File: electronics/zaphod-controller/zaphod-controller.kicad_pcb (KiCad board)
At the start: 2 copper layers, 235 parts, among them P1 MOLEX_43160-0102, P10 CONN_01X01, P11 MOLEX_MINIFIT_JR_2x4_WAY, P12 MOLEX_MINIFIT_JR_2x4_WAY, P13 MOLEX_MINIFIT_JR_2x4_WAY, P14 MOLEX_MINIFIT_JR_2x4_WAY, P17 CONN_01X02, P18 CONN_01X02, P19 CONN_01X02, P2 MOLEX_MINIFIT_JR_2x2_WAY, P20 CONN_01X06, P21 CONN_01X02, P22 CONN_01X02, P23 MOLEX_KK2.54_1x4_WAY_FAN, P3 MOLEX_MINIFIT_JR_2x2_WAY, P4 MOLEX_MINIFIT_JR_2x2_WAY, P5 MOLEX_MINIFIT_JR_2x2_WAY, P6 CONN_01X04, P7 CONN_01X04, P8 CONN_01X04, P9 CONN_01X04, Q1 Si7852DP, Q2 Si7852DP, Q3 2N7002P, Q4 NTR1P02T1G, Q5 BC847B, Q6 2N7002P, SW1 B3U-1000P_SPST-NO_SMD, SW2 B3U-1000P_SPST-NO_SMD, SW3 B3U-1000P_SPST-NO_SMD, U1 ISL85410FRZ, U10 ULN2003A, U11 ULN2003A, U2 LM5116, U3 ISL85410FRZ, U4 STM32F429VET6, U5 USBLC6, U6 ACS711KEXLT_15AB, U7 ACS711KEXLT_15AB, U8 ACS711KEXLT_15AB, U9 ACS711KEXLT_15AB, X1 CSTCE8M00G55Z, X2 SWD_SMT_SOCKET, X3 ABS06-107-32.768KHZ

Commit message: PCB layout
Mostly grouping parts and testing layout concepts
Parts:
- moved P10 131.8 mm to (113.6, 68.0)
- moved C35 106.5 mm to (183.2, 86.6)
- moved C41 104.4 mm to (169.0, 89.2)
- moved FID1 100.0 mm to (227.7, 139.3)
- moved FID2 100.0 mm to (236.2, 137.6)
- moved FID3 100.0 mm to (229.4, 135.6)
- moved FID4 100.0 mm to (232.7, 136.3)
- moved R56 95.4 mm to (157.2, 115.0), turned to 180 degrees
- moved C48 92.7 mm to (181.6, 96.8)
- moved TEST8 90.2 mm to (165.2, 76.8)
- moved SW1 88.1 mm to (170.2, 105.6), turned to 180 degrees
- moved C45 86.4 mm to (179.8, 87.2), turned to 270 degrees
- moved D5 85.8 mm to (180.2, 118.6), turned to 90 degrees
- moved X1 85.7 mm to (178.2, 92.4), turned to 90 degrees
- moved C34 85.1 mm to (156.8, 80.0), turned to 180 degrees
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
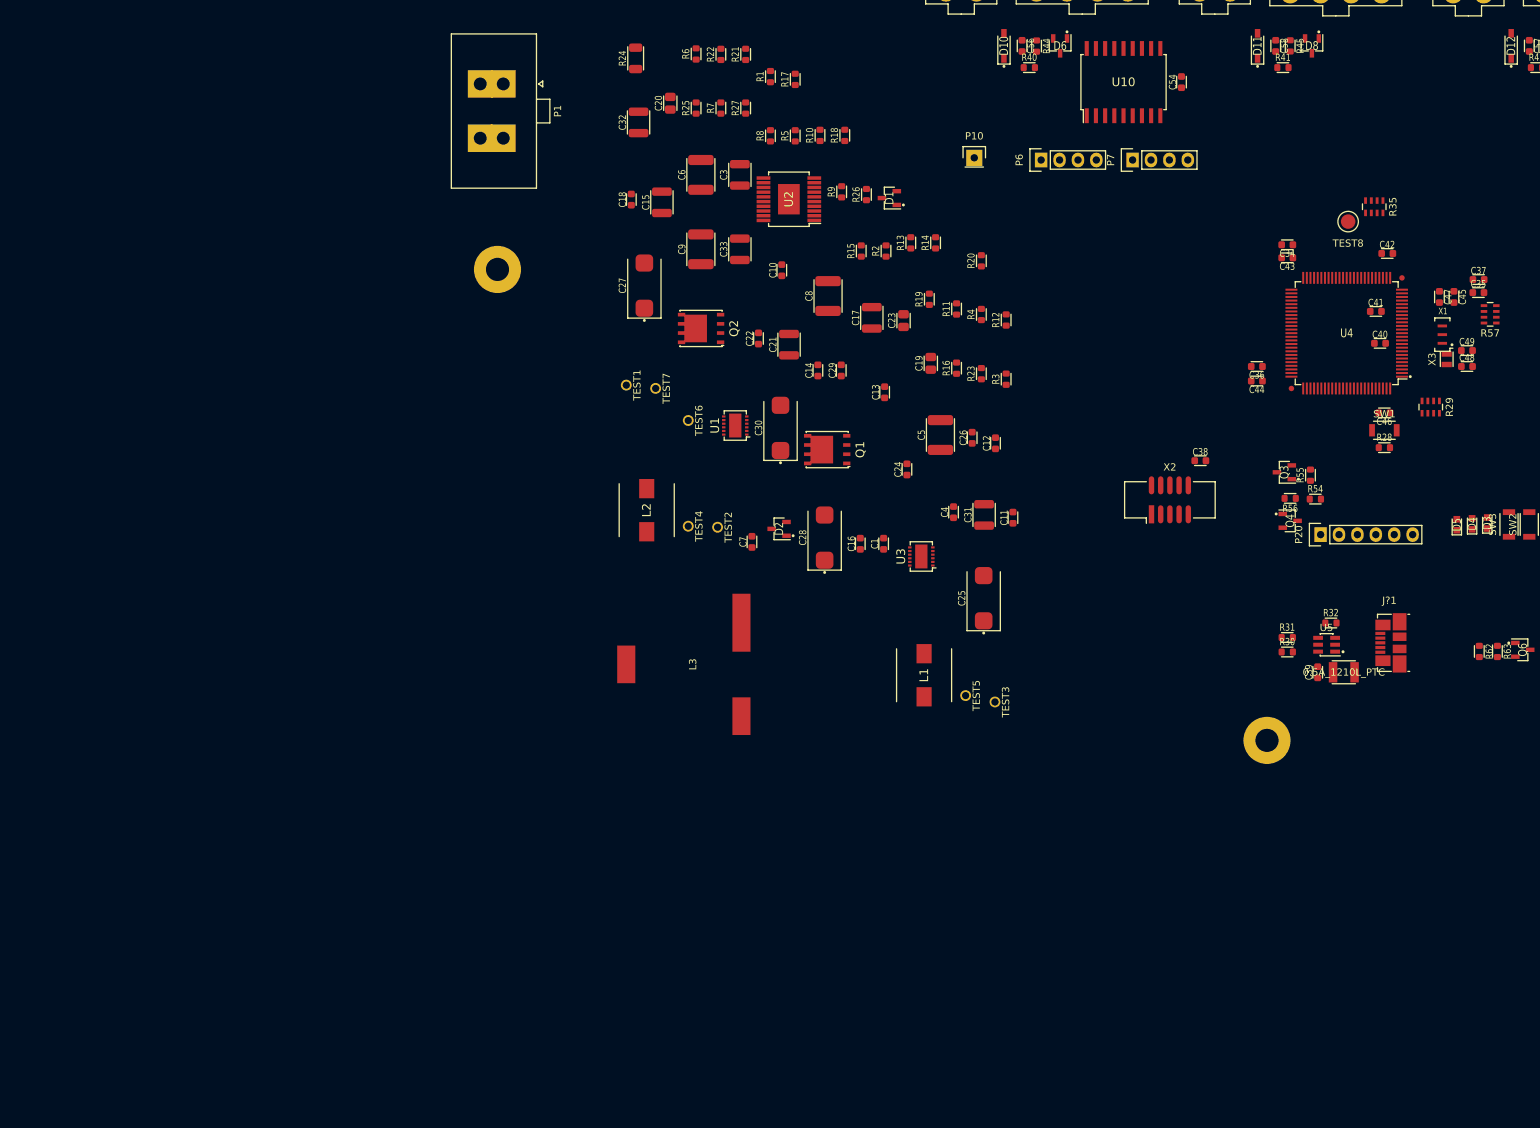
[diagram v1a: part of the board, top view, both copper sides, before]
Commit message: Placement refinement of 1A regulators
Removed some redundant parts, placed 3 and 5V regs.
Conjoined a few 1k resistors into quad arrays.
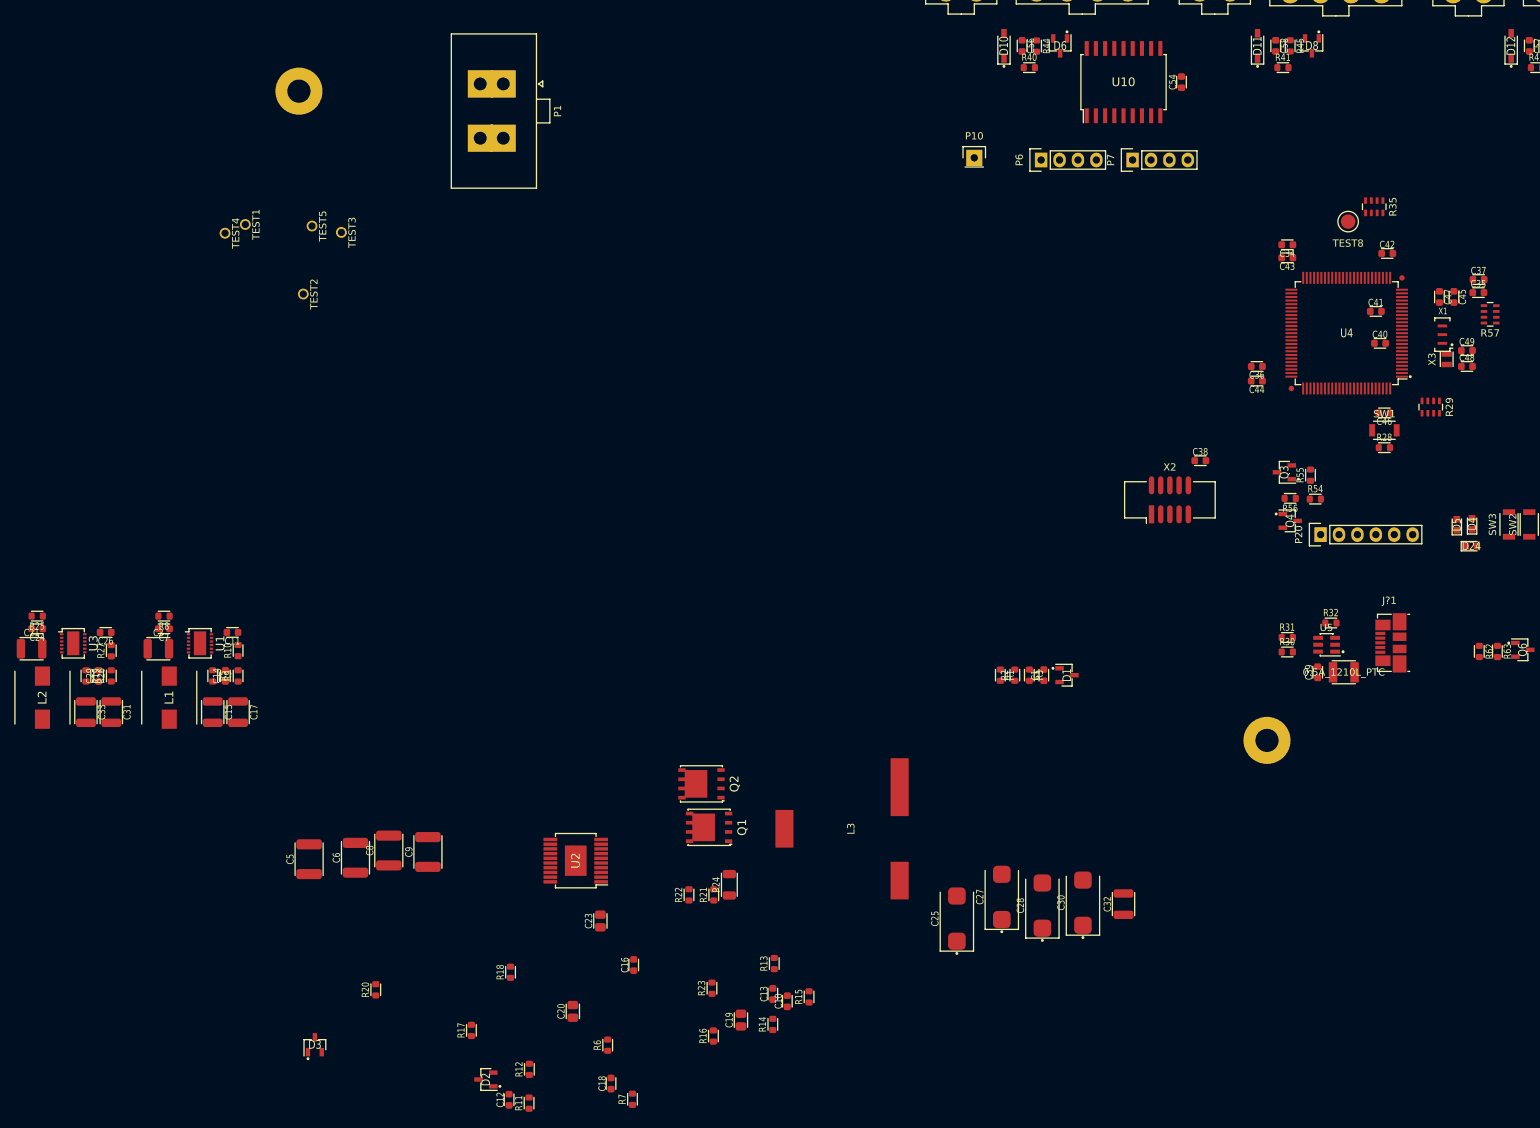
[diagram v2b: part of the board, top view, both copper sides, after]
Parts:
- removed C22, C4: 100n_X7R_1608M, Applidyne_Capacitor:CAPC1608X90N
- removed R4: 1K00_1608M, Applidyne_Resistor:RESC1608X50N
- removed TEST6, TEST7: CLIP_HOOK_WHITE, Applidyne_Test:KEYSTONE_5002
- added D24: LED_RED_1608M, Applidyne_LED:LEDC1608X80L40N, F.Cu at (182.2, 121.6)
- D3: value LED_RED_1608M -> 200V_350mW_SOT23; footprint Applidyne_LED:LEDC1608X80L40N -> Applidyne_SOT:SOT95P240X110-3L16N
- moved D3 177.1 mm to (22.6, 190.4), turned to 0 degrees
- moved R17 138.7 mm to (44.2, 188.4)
- moved R6 137.3 mm to (63.0, 190.5)
- moved R7 137.3 mm to (66.4, 197.9)
- moved R20 130.8 mm to (31.0, 182.8)
- moved R19 127.5 mm to (-9.00, 139.5), turned to 270 degrees
- moved C32 127.0 mm to (134.2, 171.0)
- moved C20 126.1 mm to (58.2, 185.8)
- moved R11 124.5 mm to (52.2, 198.5)
- moved R18 124.4 mm to (49.6, 180.4)
- moved R26 123.6 mm to (-5.50, 139.5)
- moved C31 123.5 mm to (-5.50, 144.5), turned to 270 degrees
- moved R12 122.6 mm to (52.2, 193.8)
- moved C26 122.6 mm to (-6.28, 133.5), turned to 180 degrees
- moved C24 122.0 mm to (-15.7, 133.0), turned to 180 degrees
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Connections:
- D2 pad 2: Net-(C19-Pad2) -> (no net)
- D2 pad 3: Net-(C23-Pad2) -> +POWER
- R29 pad 8: Net-(D3-PadA) -> Net-(D24-PadA)
- R57 pad 4: (no net) -> VOLTAGE_INPUT
- R57 pad 5: (no net) -> Net-(C1-Pad1)
- U1 pad 8: Net-(TEST6-Pad1) -> (no net)
- U3 pad 8: Net-(TEST7-Pad1) -> (no net)

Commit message: Layout of 75-12V regulator parts
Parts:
- added C2: 47u_ELEC_100V_1350X1350M, Applidyne_Capacitor:CAPAE1350X1350D1490DD450L470N, F.Cu at (69.8, 116.0)
- R20: moved to B.Cu
- moved R1 159.9 mm to (259.1, 65.7), turned to 180 degrees
- moved R2 157.2 mm to (259.1, 67.7), turned to 0 degrees
- moved R3 154.5 mm to (259.1, 69.7), turned to 180 degrees
- moved C1 151.8 mm to (259.1, 71.7), turned to 0 degrees
- moved D1 147.5 mm to (259.1, 74.9), turned to 180 degrees
- moved TEST4 117.8 mm to (85.5, 169.0)
- moved C12 107.3 mm to (46.5, 90.8), turned to 0 degrees
- moved R11 106.0 mm to (50.0, 92.5), turned to 180 degrees
- moved R7 105.6 mm to (46.5, 94.2), turned to 0 degrees
- moved D2 105.5 mm to (50.2, 89.8), turned to 270 degrees
- moved D3 105.5 mm to (70.8, 96.5)
- moved C19 101.7 mm to (58.0, 88.0), turned to 0 degrees
- moved TEST3 101.6 mm to (67.8, 171.0)
- moved R12 101.5 mm to (46.5, 92.5), turned to 180 degrees
- moved R16 101.1 mm to (58.0, 90.0), turned to 180 degrees
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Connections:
- D2 pad 1: Net-(C12-Pad2) -> (no net)
- D2 pad 2: (no net) -> Net-(C12-Pad2)
- L3 pad 1: +12V -> Net-(C23-Pad1)
- L3 pad 2: Net-(C23-Pad1) -> +12V

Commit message: Worked out 'final' pcb shape and finished prelim placement
Most parts are placed in groups, roughly where they should be, on their seemingly best layers etc.
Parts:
- removed MNT2, MNT4, MNT6: MNT_M3_PLATED, Applidyne_Mount:MTGP650H330
- removed P21: CONN_01X02, Applidyne_Connector_Wurth:61300211121
- removed P6, P7, P8, P9: CONN_01X04, Applidyne_Connector_Wurth:61300411121
- C1, C19, C50, C51, C52, C53, C54, C55, C56, C57, C58, C59, C60, C61, C62, C63, C64, C66, C67, C68, C69, C72, C74, D1, D10, D11, D12, D13, D14, D15, D16, D17, D18, D19, D20, D21, D22, D23, D6, D7, D8, D9, F2, P10, Q5, Q6, R1, R16, R2, R3, R33, R34, R36, R37, R38, R39, R40, R41, R42, R43, R44, R45, R46, R47, R48, R49, R50, R51, R52, R53, R59, R60, R61, R62, R63, R64, R65, R66, TEST8, U10, U11, U6, U7, U8, U9: moved to B.Cu
- moved FID1 188.3 mm to (54.6, 65.2)
- moved FID3 106.0 mm to (149.9, 65.5)
- moved FID2 89.4 mm to (149.8, 114.6)
- moved TEST3 88.5 mm to (134.0, 112.3)
- moved C21 84.7 mm to (129.5, 97.2)
- moved C24 84.7 mm to (130.3, 94.5)
- moved C26 84.7 mm to (139.7, 95.0)
- moved C29 84.7 mm to (138.8, 101.0)
- moved C31 84.7 mm to (140.5, 106.0)
- moved C33 84.7 mm to (137.0, 106.0)
- moved L2 84.7 mm to (131.0, 104.0)
- moved R19 84.7 mm to (137.0, 101.0)
- moved R25 84.7 mm to (130.3, 92.8)
- moved R26 84.7 mm to (140.5, 101.0)
- moved R27 84.7 mm to (140.5, 97.5)
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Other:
- board outline added: 199.9 x 69.3 mm

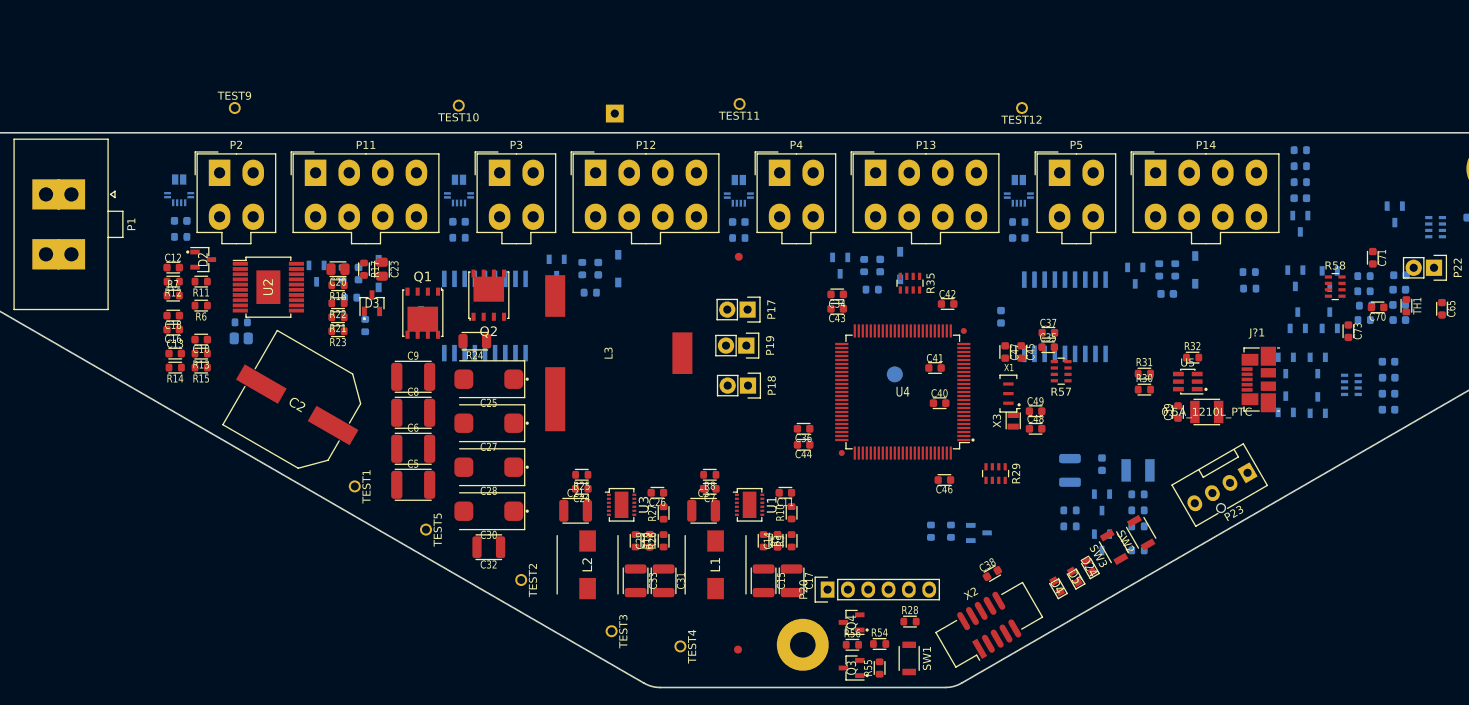
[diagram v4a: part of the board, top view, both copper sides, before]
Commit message: Routing and layout improvements
Reworked some pinouts/connector assignments, part switching etc.
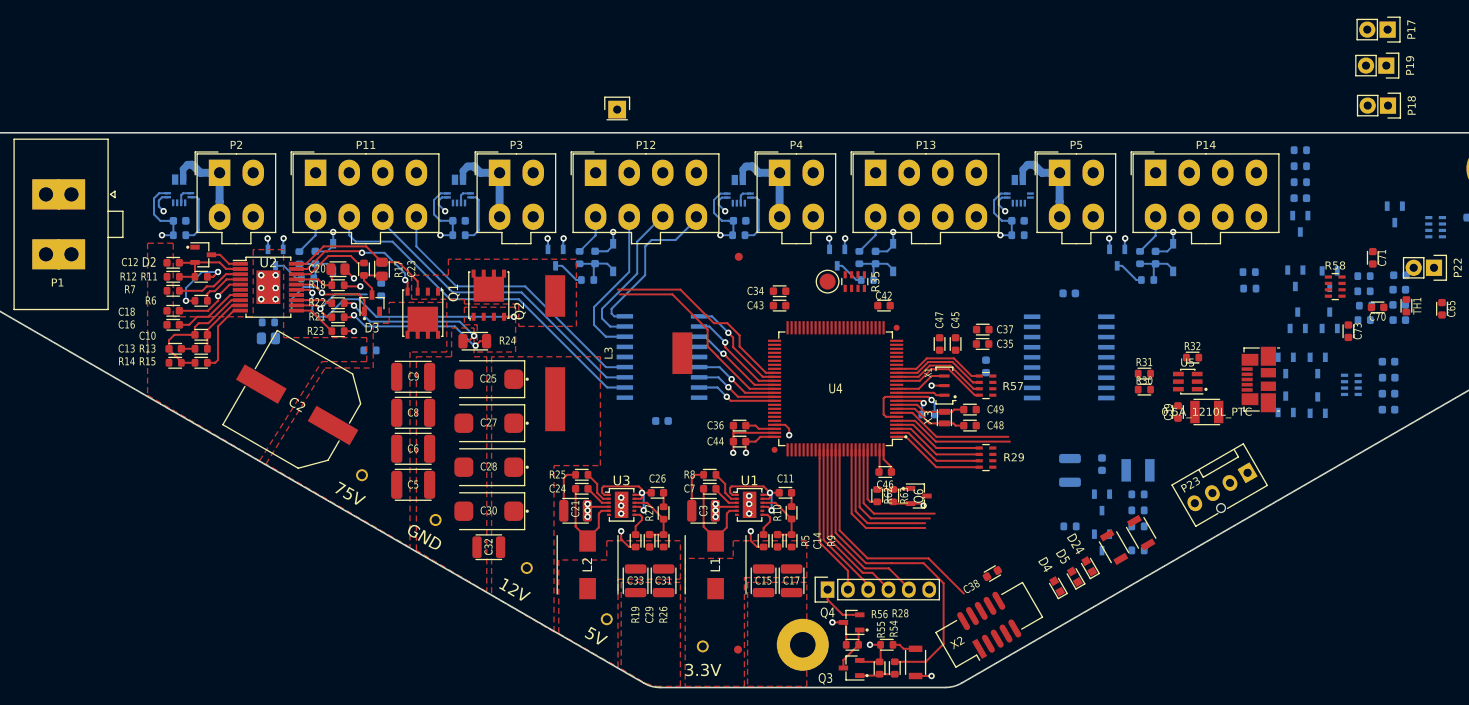
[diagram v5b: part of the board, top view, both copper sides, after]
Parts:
- removed R59: 1K00_1608M, Applidyne_Resistor:RESC1608X50N
- removed TEST10, TEST11, TEST12, TEST9: CLIP_HOOK_PURPLE, Applidyne_Test:KEYSTONE_5119
- added TH2: NTC_10K_1608M, Applidyne_Resistor:RESC1608X50N, B.Cu at (103.8, 77.2)
- C40, C41: moved to B.Cu
- P10, Q6, R62, R63, TEST8: moved to F.Cu
- moved P17 87.3 mm to (231.0, 37.1)
- moved P18 87.3 mm to (231.1, 46.6)
- moved P19 87.3 mm to (230.8, 41.6)
- moved C54 32.9 mm to (140.3, 86.0), turned to 180 degrees
- moved U10 22.7 mm to (140.3, 78.0), turned to 270 degrees
- moved TEST8 14.3 mm to (161.0, 68.6)
- moved R57 9.57 mm to (180.8, 81.6)
- moved C55 9.02 mm to (191.2, 70.1), turned to 0 degrees
- moved Q6 8.83 mm to (172.4, 95.4), turned to 270 degrees
- moved X3 8.61 mm to (175.6, 85.6)
- moved R63 8.48 mm to (169.2, 95.4), turned to 270 degrees
- moved U4 8.41 mm to (162.0, 82.0)
- moved C45 8.26 mm to (177.0, 76.4)
- moved C47 8.26 mm to (175.0, 76.4)
- moved C35 8.21 mm to (180.4, 76.4)
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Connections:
- Q6 pad 3: (no net) -> Net-(Q6-Pad3)
- R29 pad 1: STATUS_0 -> FAN_HALL
- R29 pad 2: STATUS_1 -> STATUS_0
- R29 pad 3: STATUS_2 -> STATUS_1
- R29 pad 4: (no net) -> STATUS_2
- R29 pad 5: (no net) -> Net-(D5-PadA)
- R29 pad 6: Net-(D5-PadA) -> Net-(D4-PadA)
- R29 pad 7: Net-(D4-PadA) -> Net-(D24-PadA)
- R29 pad 8: Net-(D24-PadA) -> Net-(D23-Pad3)
- R57 pad 4: VOLTAGE_INPUT -> Net-(C1-Pad1)
- R57 pad 5: Net-(C1-Pad1) -> VOLTAGE_INPUT
- R58 pad 4: (no net) -> Net-(R58-Pad4)
- R58 pad 5: (no net) -> Net-(R58-Pad5)
- U1 pad 8: (no net) -> Net-(U1-Pad8)
- U10 pad 1: SERVO1_B -> SERVO2_EN
- U10 pad 11: (no net) -> Net-(P11-Pad6)
- U10 pad 12: (no net) -> Net-(P11-Pad7)
- U10 pad 13: Net-(P12-Pad8) -> Net-(P11-Pad8)
- U10 pad 14: Net-(P12-Pad7) -> Net-(U10-Pad14)
- U10 pad 15: Net-(P12-Pad6) -> Net-(U10-Pad15)
- U10 pad 16: Net-(P11-Pad8) -> Net-(P12-Pad6)
- U10 pad 17: Net-(P11-Pad7) -> Net-(P12-Pad7)
- U10 pad 18: Net-(P11-Pad6) -> Net-(P12-Pad8)
- U10 pad 2: SERVO1_A -> SERVO2_A
- U10 pad 3: SERVO1_EN -> SERVO2_B
- U10 pad 4: SERVO2_B -> Net-(U10-Pad4)
- U10 pad 5: SERVO2_A -> Net-(U10-Pad5)
- U10 pad 6: SERVO2_EN -> SERVO1_EN
- U10 pad 7: (no net) -> SERVO1_A
- U10 pad 8: (no net) -> SERVO1_B
- U11 pad 1: SERVO3_B -> SERVO4_EN
- U11 pad 11: (no net) -> Net-(P13-Pad6)
- U11 pad 12: (no net) -> Net-(P13-Pad7)
- U11 pad 13: Net-(P14-Pad8) -> Net-(P13-Pad8)
- U11 pad 14: Net-(P14-Pad7) -> Net-(U11-Pad14)
- U11 pad 15: Net-(P14-Pad6) -> Net-(U11-Pad15)
- U11 pad 16: Net-(P13-Pad8) -> Net-(P14-Pad6)
- U11 pad 17: Net-(P13-Pad7) -> Net-(P14-Pad7)
- U11 pad 18: Net-(P13-Pad6) -> Net-(P14-Pad8)
- U11 pad 2: SERVO3_A -> SERVO4_A
- U11 pad 3: SERVO3_EN -> SERVO4_B
- U11 pad 4: SERVO4_B -> Net-(U11-Pad4)
- U11 pad 5: SERVO4_A -> Net-(U11-Pad5)
- U11 pad 6: SERVO4_EN -> SERVO3_EN
- U11 pad 7: (no net) -> SERVO3_A
- U11 pad 8: (no net) -> SERVO3_B
- U3 pad 8: (no net) -> Net-(U3-Pad8)
- U4 pad 41: (no net) -> Net-(U4-Pad41)
- U4 pad 42: (no net) -> Net-(U4-Pad42)
- U4 pad 46: (no net) -> Net-(U4-Pad46)
- U4 pad 51: (no net) -> Net-(U4-Pad51)
- U4 pad 52: (no net) -> Net-(U4-Pad52)
- U4 pad 55: (no net) -> Net-(U4-Pad55)
- U4 pad 56: (no net) -> Net-(U4-Pad56)
- U4 pad 57: (no net) -> Net-(U4-Pad57)
- U4 pad 58: (no net) -> Net-(U4-Pad58)
- U4 pad 67: (no net) -> Net-(U4-Pad67)
- U4 pad 78: (no net) -> Net-(U4-Pad78)
- U4 pad 79: (no net) -> Net-(U4-Pad79)
- U4 pad 80: (no net) -> EXT_OUTPUT_0
- U4 pad 81: (no net) -> EXT_INPUT_1
- U4 pad 82: (no net) -> EXT_OUTPUT_1
- U4 pad 83: (no net) -> EXT_INPUT_0
- U4 pad 90: (no net) -> Net-(U4-Pad90)
- U4 pad 91: (no net) -> Net-(U4-Pad91)
- U4 pad 97: (no net) -> Net-(U4-Pad97)
- U4 pad 98: (no net) -> Net-(U4-Pad98)
- X2 pad 7: (no net) -> Net-(X2-Pad7)
- X2 pad 8: (no net) -> Net-(X2-Pad8)
- X2 pad 9: (no net) -> Net-(X2-Pad9)
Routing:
- net GND: track 0.00 -> 94.6 mm, vias 0 -> 29
- net +3.3V: track 0.00 -> 71.5 mm, vias 0 -> 12
- net Net-(P11-Pad6): track 0.00 -> 44.6 mm
- net USART_2_PWR_EN: track 0.00 -> 41.1 mm
- net Net-(P11-Pad7): track 0.00 -> 39.0 mm
- net Net-(P11-Pad8): track 0.00 -> 36.0 mm
- net Net-(Q2-Pad1): track 0.00 -> 33.1 mm, vias 0 -> 2
- net SERVO1_HLFB: track 0.00 -> 29.4 mm
- net SWO: track 0.00 -> 28.9 mm
- net SERVO2_HLFB: track 0.00 -> 28.6 mm
- net +12V: track 0.00 -> 23.5 mm, vias 0 -> 9
- net USART_2_RX: track 0.00 -> 23.2 mm
- net USART_2_TX: track 0.00 -> 21.3 mm
- net Net-(P12-Pad8): track 0.00 -> 20.0 mm
- net Net-(P12-Pad6): track 0.00 -> 19.8 mm
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- added copper zone on F.Cu, net +12V
- added copper zone on F.Cu, net +3.3V
- added copper zone on F.Cu, net +5V
- added copper zone on F.Cu, net +POWER
- added copper zone on F.Cu, net GND
- added copper zone on F.Cu, net Net-(C23-Pad1)
- added copper zone on F.Cu, net Net-(Q2-Pad2)
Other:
- copper layers 2 -> 4
- board text added: "12V"
- board text added: "3.3V"
- board text added: "5V"
- board text added: "75V"
- board text added: "GND"
